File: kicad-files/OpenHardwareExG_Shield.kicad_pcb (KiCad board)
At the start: 4 copper layers, 125.1 x 59.7 mm, 196 parts, among them P1 CONN_1, P10 CONN_18, P11 CONN_1, P12 CONN_1, P13 CONN_1, P14 CONN_1, P15 CONN_1, P16 CONN_1, P17 CONN_1, P18 CONN_1, P19 ARDUINO_SHIELD, P2 CONN_1, P20 CONN_3X2, P21 CONN_3X2, P22 CONN_7, P23 CONN_1, P24 CONN_1, P25 CONN_1, P26 CONN_1, P27 CONN_1, P28 CONN_1, P29 CONN_1, P3 CONN_1, P30 CONN_1, P31 CONN_1, P32 CONN_1, P33 CONN_1, P34 CONN_1, P35 CONN_1, P36 CONN_1, P37 CONN_1, P38 CONN_1, P39 CONN_1, P4 CONN_1, P40 CONN_1, P41 CONN_1, P42 CONN_1, P43 CONN_1, P44 CONN_1, P45 CONN_1, P46 CONN_1, P47 CONN_1, P48 CONN_1, P49 CONN_1, P5 CONN_1, P50 CONN_1, P51 CONN_1, P52 CONN_1, P53 CONN_1, P54 CONN_1, P55 CONN_1, P6 CONN_1, P7 CONN_1, P8 CONN_1, P9 CONN_1, U1 ADS1299, U2 Z0109MNT1G, U3 TL431BIDBZR, U4 873-AAT3220IGY-33T1, U5 ADUM6000, U6 SI8663, U7 74LS02, U8 74LS00, U9 74LS125

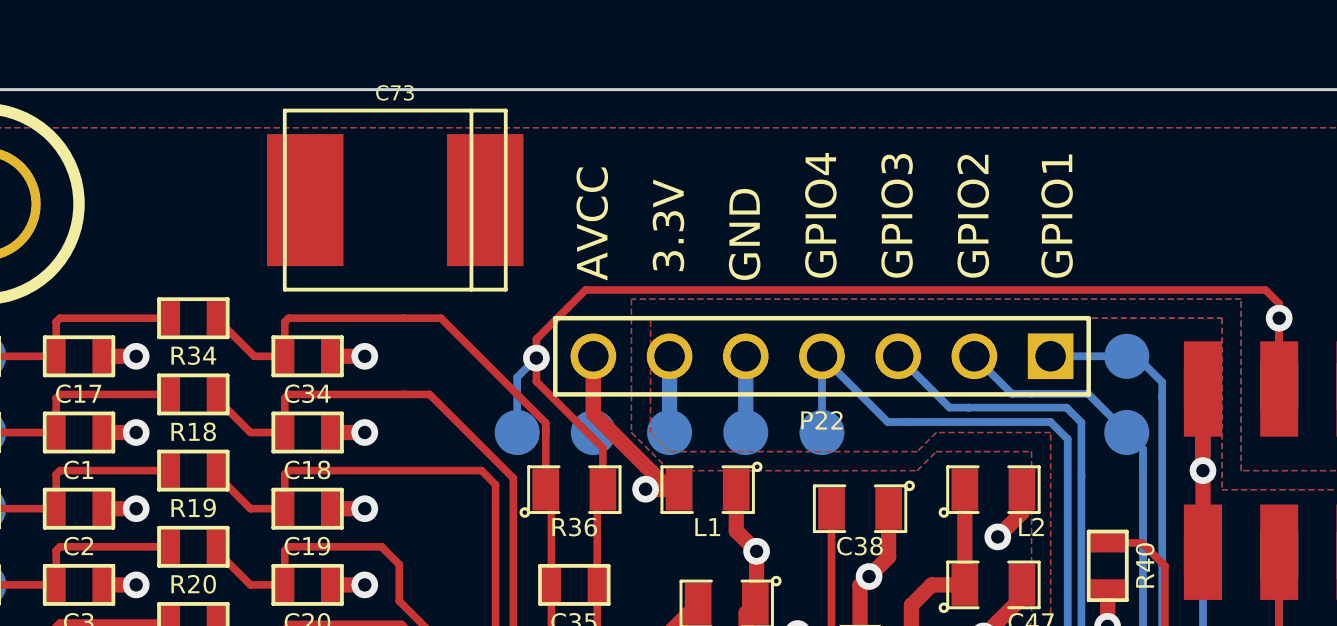
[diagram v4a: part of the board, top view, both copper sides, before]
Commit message: add C73 (330uF) to PCB
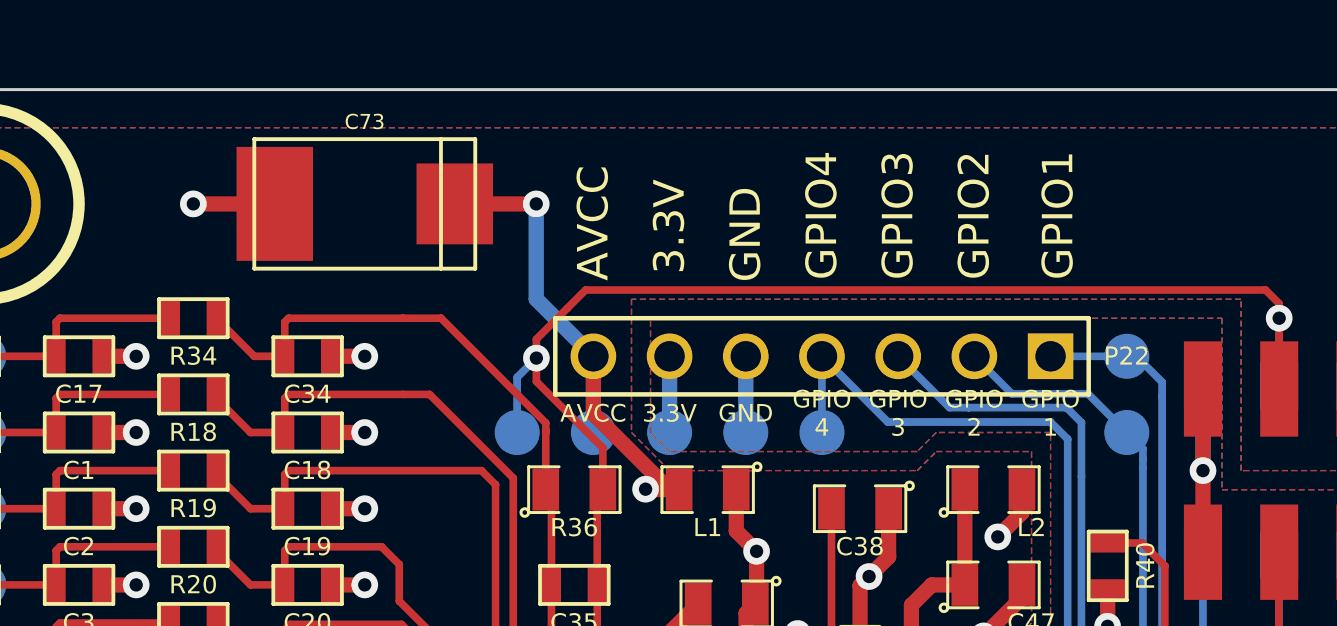
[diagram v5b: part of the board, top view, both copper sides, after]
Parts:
- C73: footprint c_tant_E -> c_tant_D
- moved C73 1.02 mm to (81.3, 33.0)
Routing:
- net /VIN_ISO: track 46.9 -> 55.5 mm, vias 7 -> 8
- net AGND: track 157.3 -> 160.0 mm, vias 64 -> 65
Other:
- board text added: "GPIO 1"
- board text added: "GPIO 2"
- board text added: "GPIO 3"
- board text added: "GPIO 4"
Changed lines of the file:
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@@
   (general
     (links 374)
-    (no_connects 1)
-    (area 59.004999 29.159999 184.200001 88.950001)
+    (no_connects 0)
+    (area 59.004999 28.0083 184.7167 91.2876)
     (thickness 1.6)
-    (drawings 53)
-    (tracks 1164)
+    (drawings 67)
+    (tracks 1170)
     (zones 0)
     (modules 196)
@@
     (2 Inner2.Cu power hide)
     (1 Inner1.Cu power hide)
-    (0 B.Cu signal hide)
+    (0 B.Cu signal)
     (16 B.Adhes user)
     (17 F.Adhes user)
@@
     (pad_to_mask_clearance 0)
     (aux_axis_origin 0 0)
-    (visible_elements 7FFFF73F)
+    (visible_elements 7FFFFF3F)
     (pcbplotparams
       (layerselection 3145728)
@@
   (module PIN_ARRAY_7x1 (layer F.Cu)
     (at 96.52 38.1 180)
-    (fp_text reference P22 (at 0 -2.159 180) (layer F.SilkS)
+    (fp_text reference P22 (at -10.16 0 180) (layer F.SilkS)
       (effects (font (size 0.6 0.6) (thickness 0.127)))
     )
@@
     )
   )
-  (module c_tant_E (layer F.Cu)
-    (at 82.296 32.893)
-    (descr "SMT capacitor, tantalum size E")
-    (fp_text reference C73 (at 0 -3.556) (layer F.SilkS)
+  (module c_tant_D (layer F.Cu)
+    (at 81.28 33.02)
+    (descr "SMT capacitor, tantalum size D")
+    (fp_text reference C73 (at 0 -2.7305) (layer F.SilkS)
       (effects (font (size 0.50038 0.50038) (thickness 0.11938)))
     )
-    (fp_text value 330uF (at 0 3.556) (layer F.SilkS) hide
+    (fp_text value 330uF (at 0 2.7305) (layer F.SilkS) hide
       (effects (font (size 0.50038 0.50038) (thickness 0.11938)))
     )
-    (fp_line (start 3.683 -2.9845) (end 3.683 2.9845) (layer F.SilkS) (width 0.127))
-    (fp_line (start 2.54 2.9845) (end 2.54 -2.9845) (layer F.SilkS) (width 0.127))
-    (fp_line (start -3.683 -2.9845) (end -3.683 2.9845) (layer F.SilkS) (width 0.127))
-    (fp_line (start -3.683 2.9845) (end 3.683 2.9845) (layer F.SilkS) (width 0.127))
-    (fp_line (start 3.683 -2.9845) (end -3.683 -2.9845) (layer F.SilkS) (width 0.127))
-    (pad 1 smd rect (at 2.99974 0) (size 2.55016 4.39928)
+    (fp_line (start 2.54 -2.159) (end 2.54 2.159) (layer F.SilkS) (width 0.127))
+    (fp_line (start -3.683 -2.159) (end -3.683 2.159) (layer F.SilkS) (width 0.127))
+    (fp_line (start -3.683 2.159) (end 3.683 2.159) (layer F.SilkS) (width 0.127))
+    (fp_line (start 3.683 2.159) (end 3.683 -2.159) (layer F.SilkS) (width 0.127))
+    (fp_line (start 3.683 -2.159) (end -3.683 -2.159) (layer F.SilkS) (width 0.127))
+    (pad 1 smd rect (at 2.99974 0) (size 2.55016 2.70002)
       (layers F.Cu F.Paste F.Mask)
       (net 53 /VIN_ISO)
     )
-    (pad 2 smd rect (at -2.99974 0) (size 2.55016 4.39928)
+    (pad 2 smd rect (at -2.99974 0) (size 2.55016 3.79984)
       (layers F.Cu F.Paste F.Mask)
       (net 57 AGND)
     )
-    (model smd/capacitors/c_tant_E.wrl
+    (model smd/capacitors/c_tant_D.wrl
       (at (xyz 0 0 0))
       (scale (xyz 1 1 1))
@@
     )
   )
+  (gr_text "GPIO\n1" (at 104.14 40.005) (layer F.SilkS)
+    (effects (font (size 0.5842 0.5842) (thickness 0.127)))
+  )
+  (gr_text "GPIO\n2" (at 101.6 40.005) (layer F.SilkS)
+    (effects (font (size 0.5842 0.5842) (thickness 0.127)))
+  )
+  (gr_text "GPIO\n3" (at 99.06 40.005) (layer F.SilkS)
+    (effects (font (size 0.5842 0.5842) (thickness 0.127)))
+  )
+  (gr_text "GPIO\n4" (at 96.52 40.005) (layer F.SilkS)
+    (effects (font (size 0.5842 0.5842) (thickness 0.127)))
+  )
+  (gr_text GND (at 93.98 40.005) (layer F.SilkS)
+    (effects (font (size 0.5842 0.5842) (thickness 0.127)))
+  )
+  (gr_text 3.3V (at 91.44 40.005) (layer F.SilkS)
+    (effects (font (size 0.5842 0.5842) (thickness 0.127)))
+  )
+  (gr_text AVCC (at 88.9 40.005) (layer F.SilkS)
+    (effects (font (size 0.5842 0.5842) (thickness 0.127)))
+  )
+  (gr_text 3.3V (at 91.44 33.782 90) (layer F.SilkS)
+    (effects (font (size 1.016 1.016) (thickness 0.2032)))
+  )
+  (gr_text GND (at 93.98 34.036 90) (layer B.SilkS)
+    (effects (font (size 1.016 1.016) (thickness 0.2032)) (justify mirror))
+  )
+  (gr_text GPIO4 (at 96.52 33.401 90) (layer B.SilkS)
+    (effects (font (size 1.016 1.016) (thickness 0.2032)) (justify mirror))
+  )
+  (gr_text GPIO3 (at 99.06 33.401 90) (layer B.SilkS)
+    (effects (font (size 1.016 1.016) (thickness 0.2032)) (justify mirror))
+  )
+  (gr_text GPIO2 (at 101.6 33.401 90) (layer B.SilkS)
+    (effects (font (size 1.016 1.016) (thickness 0.2032)) (justify mirror))
+  )
+  (gr_text GPIO1 (at 104.394 33.401 90) (layer B.SilkS)
+    (effects (font (size 1.016 1.016) (thickness 0.2032)) (justify mirror))
+  )
+  (gr_text AVCC (at 88.9 33.655 90) (layer B.SilkS)
+    (effects (font (size 1.016 1.016) (thickness 0.2032)) (justify mirror))
+  )
   (gr_text "rev. 0.0" (at 154.94 78.74) (layer F.SilkS)
     (effects (font (size 1.016 1.016) (thickness 0.2032)))
@@
     (effects (font (size 1.016 1.016) (thickness 0.2032)))
   )
-  (gr_text 3.3V (at 91.44 33.782 90) (layer F.SilkS)
-    (effects (font (size 1.016 1.016) (thickness 0.2032)))
+  (gr_text 3.3V (at 91.44 33.782 90) (layer B.SilkS)
+    (effects (font (size 1.016 1.016) (thickness 0.2032)) (justify mirror))
   )
   (gr_text AVCC (at 88.9 33.655 90) (layer F.SilkS)
@@
   (segment (start 153.58 61.52) (end 135.76 61.52) (width 0.254) (layer F.Cu) (net 52))
   (segment (start 157.465 65.405) (end 153.58 61.52) (width 0.254) (layer F.Cu) (net 52))
+  (segment (start 88.9 38.1) (end 86.995 36.195) (width 0.508) (layer B.Cu) (net 53))
+  (segment (start 86.995 33.02) (end 84.27974 33.02) (width 0.508) (layer F.Cu) (net 53))
+  (via (at 86.995 33.02) (size 0.889) (layers F.Cu B.Cu) (net 53))
+  (segment (start 86.995 36.195) (end 86.995 33.02) (width 0.508) (layer B.Cu) (net 53))
   (segment (start 91.7575 42.545) (end 90.655 42.545) (width 0.508) (layer F.Cu) (net 53))
   (via (at 90.64 42.53) (size 0.889) (layers F.Cu B.Cu) (net 53))
@@
   (segment (start 167.64 48.26) (end 161.925 48.26) (width 0.254) (layer F.Cu) (net 56))
   (segment (start 168.275 48.895) (end 167.64 48.26) (width 0.254) (layer F.Cu) (net 56))
+  (segment (start 78.28026 33.02) (end 75.565 33.02) (width 0.508) (layer F.Cu) (net 57))
+  (via (at 75.565 33.02) (size 0.889) (layers F.Cu B.Cu) (net 57))
   (segment (start 100.0125 60.94222) (end 98.40722 60.94222) (width 0.254) (layer F.Cu) (net 57))
   (via (at 98.298 60.833) (size 0.889) (layers F.Cu B.Cu) (net 57))

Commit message: version bump to r0.1
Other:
- board text added: "rev. 0.1"
- board text removed: "rev. 0.0"
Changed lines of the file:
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@@
     (visible_elements 7FFFFF3F)
     (pcbplotparams
-      (layerselection 3145728)
+      (layerselection 284983303)
       (usegerberextensions true)
       (excludeedgelayer true)
@@
     (effects (font (size 1.016 1.016) (thickness 0.2032)) (justify mirror))
   )
-  (gr_text "rev. 0.0" (at 154.94 78.74) (layer F.SilkS)
+  (gr_text "rev. 0.1" (at 154.94 78.74) (layer F.SilkS)
     (effects (font (size 1.016 1.016) (thickness 0.2032)))
   )
-  (gr_text "rev. 0.0" (at 154.94 78.74) (layer B.SilkS)
+  (gr_text "rev. 0.1" (at 154.94 78.74) (layer B.SilkS)
     (effects (font (size 1.016 1.016) (thickness 0.2032)) (justify mirror))
   )

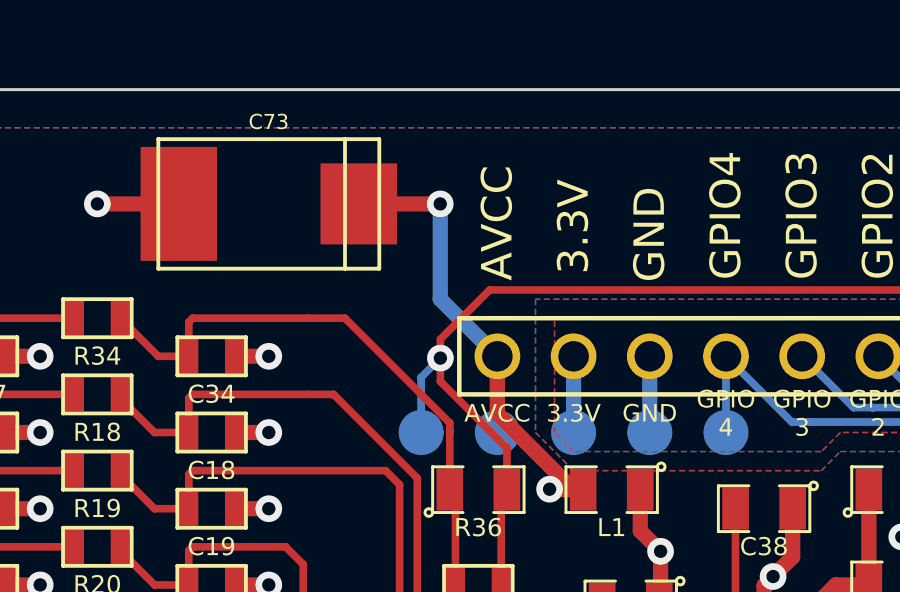
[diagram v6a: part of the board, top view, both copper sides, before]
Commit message: move via for C73 to the power plane
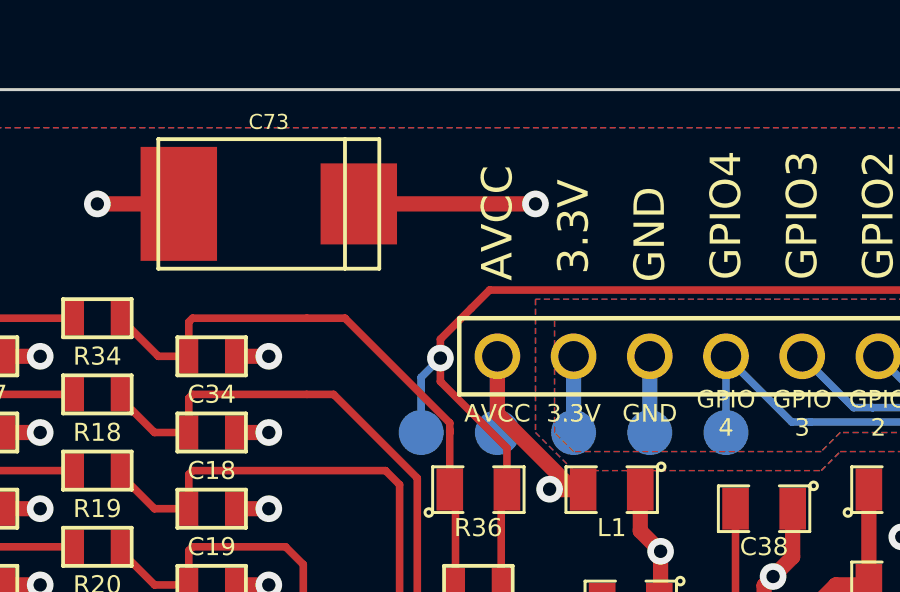
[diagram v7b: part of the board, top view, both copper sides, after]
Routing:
- net /VIN_ISO: track 55.5 -> 52.8 mm
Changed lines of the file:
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@@
     (thickness 1.6)
     (drawings 67)
-    (tracks 1170)
+    (tracks 1168)
     (zones 0)
     (modules 196)
@@
   (layers
     (15 F.Cu signal)
-    (2 Inner2.Cu power hide)
-    (1 Inner1.Cu power hide)
+    (2 Inner2.Cu power)
+    (1 Inner1.Cu power)
     (0 B.Cu signal)
     (16 B.Adhes user)
@@
   (segment (start 153.58 61.52) (end 135.76 61.52) (width 0.254) (layer F.Cu) (net 52))
   (segment (start 157.465 65.405) (end 153.58 61.52) (width 0.254) (layer F.Cu) (net 52))
-  (segment (start 88.9 38.1) (end 86.995 36.195) (width 0.508) (layer B.Cu) (net 53))
-  (segment (start 86.995 33.02) (end 84.27974 33.02) (width 0.508) (layer F.Cu) (net 53))
-  (via (at 86.995 33.02) (size 0.889) (layers F.Cu B.Cu) (net 53))
-  (segment (start 86.995 36.195) (end 86.995 33.02) (width 0.508) (layer B.Cu) (net 53))
+  (segment (start 90.17 33.02) (end 84.27974 33.02) (width 0.508) (layer F.Cu) (net 53))
+  (via (at 90.17 33.02) (size 0.889) (layers F.Cu B.Cu) (net 53))
   (segment (start 91.7575 42.545) (end 90.655 42.545) (width 0.508) (layer F.Cu) (net 53))
   (via (at 90.64 42.53) (size 0.889) (layers F.Cu B.Cu) (net 53))

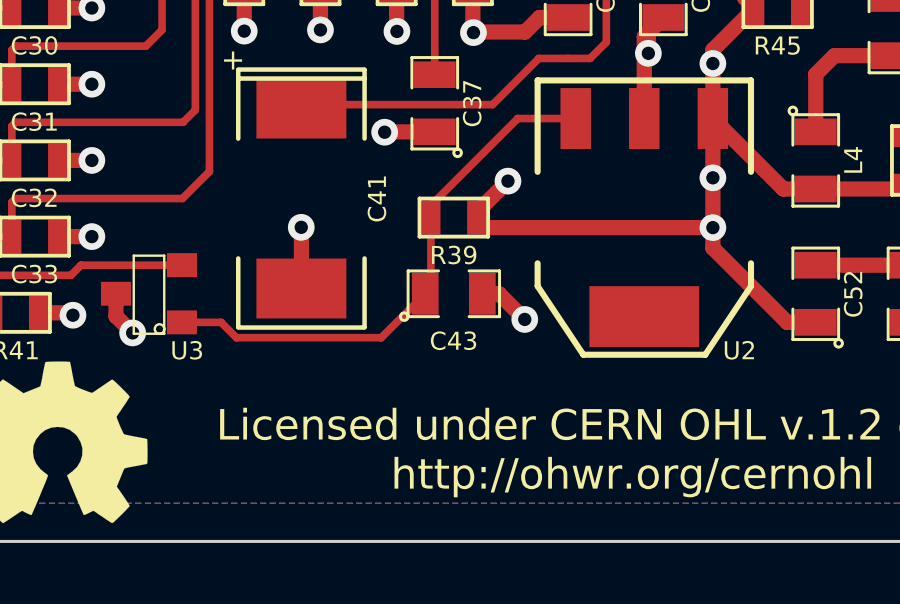
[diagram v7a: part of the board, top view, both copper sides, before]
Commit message: fix C43 footprint
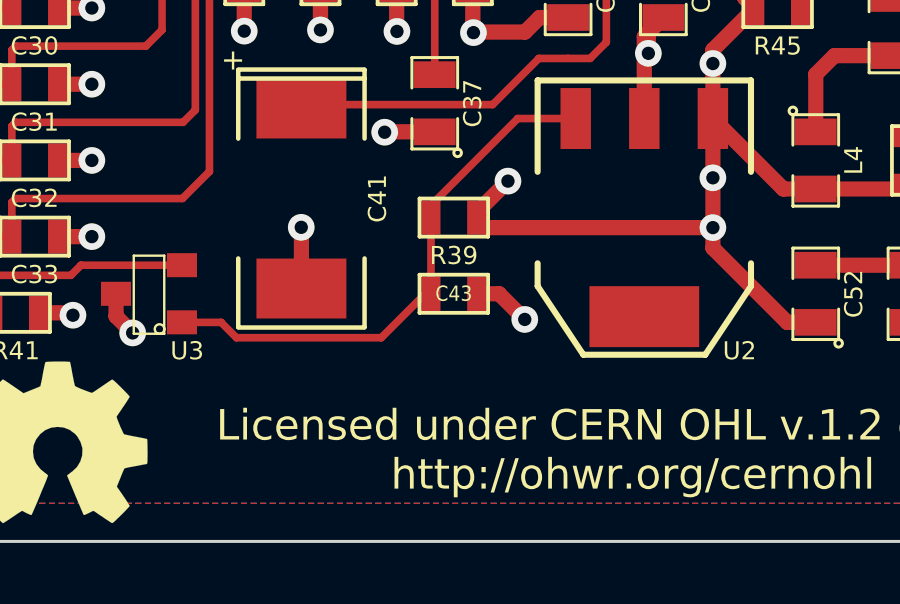
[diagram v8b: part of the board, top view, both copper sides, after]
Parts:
- C43: footprint SM0805 -> SM0603
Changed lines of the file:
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@@
   )
   (module SM0805 (layer F.Cu)
-    (at 93.345 80.645)
-    (attr smd)
-    (fp_text reference C43 (at 0 1.5875) (layer F.SilkS)
-      (effects (font (size 0.6 0.6) (thickness 0.127)))
-    )
-    (fp_text value 100nF (at 0 0.381) (layer F.SilkS) hide
-      (effects (font (size 0.50038 0.50038) (thickness 0.10922)))
-    )
-    (fp_circle (center -1.651 0.762) (end -1.651 0.635) (layer F.SilkS) (width 0.09906))
-    (fp_line (start -0.508 0.762) (end -1.524 0.762) (layer F.SilkS) (width 0.09906))
-    (fp_line (start -1.524 0.762) (end -1.524 -0.762) (layer F.SilkS) (width 0.09906))
-    (fp_line (start -1.524 -0.762) (end -0.508 -0.762) (layer F.SilkS) (width 0.09906))
-    (fp_line (start 0.508 -0.762) (end 1.524 -0.762) (layer F.SilkS) (width 0.09906))
-    (fp_line (start 1.524 -0.762) (end 1.524 0.762) (layer F.SilkS) (width 0.09906))
-    (fp_line (start 1.524 0.762) (end 0.508 0.762) (layer F.SilkS) (width 0.09906))
-    (pad 1 smd rect (at -0.9525 0) (size 0.889 1.397)
-      (layers F.Cu F.Paste F.Mask)
-      (net 91 N-0000047)
-    )
-    (pad 2 smd rect (at 0.9525 0) (size 0.889 1.397)
-      (layers F.Cu F.Paste F.Mask)
-      (net 57 AGND)
-    )
-    (model smd/chip_cms.wrl
-      (at (xyz 0 0 0))
-      (scale (xyz 0.1 0.1 0.1))
-      (rotate (xyz 0 0 0))
-    )
-  )
-  (module SM0805 (layer F.Cu)
     (at 93.345 46.355 180)
     (attr smd)
@@
       (rotate (xyz 0 0 0))
     )
+  )
+  (module SM0603 (layer F.Cu)
+    (at 93.345 80.645)
+    (attr smd)
+    (fp_text reference C43 (at 0 0) (layer F.SilkS)
+      (effects (font (size 0.508 0.4572) (thickness 0.1143)))
+    )
+    (fp_text value 100nF (at 0 0) (layer F.SilkS) hide
+      (effects (font (size 0.508 0.4572) (thickness 0.1143)))
+    )
+    (fp_line (start -1.143 -0.635) (end 1.143 -0.635) (layer F.SilkS) (width 0.127))
+    (fp_line (start 1.143 -0.635) (end 1.143 0.635) (layer F.SilkS) (width 0.127))
+    (fp_line (start 1.143 0.635) (end -1.143 0.635) (layer F.SilkS) (width 0.127))
+    (fp_line (start -1.143 0.635) (end -1.143 -0.635) (layer F.SilkS) (width 0.127))
+    (pad 1 smd rect (at -0.762 0) (size 0.635 1.143)
+      (layers F.Cu F.Paste F.Mask)
+      (net 91 N-0000047)
+    )
+    (pad 2 smd rect (at 0.762 0) (size 0.635 1.143)
+      (layers F.Cu F.Paste F.Mask)
+      (net 57 AGND)
+    )
+    (model smd\resistors\R0603.wrl
+      (at (xyz 0 0 0.001))
+      (scale (xyz 0.5 0.5 0.5))
+      (rotate (xyz 0 0 0))
+    )
